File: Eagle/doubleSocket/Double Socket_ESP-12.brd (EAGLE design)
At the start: 160 x 100 mm, 29 parts, among them IC1 LM1117IMPX-3.3, K1 G5L, K2 G5L, T1 2N3904, T2 2N3904

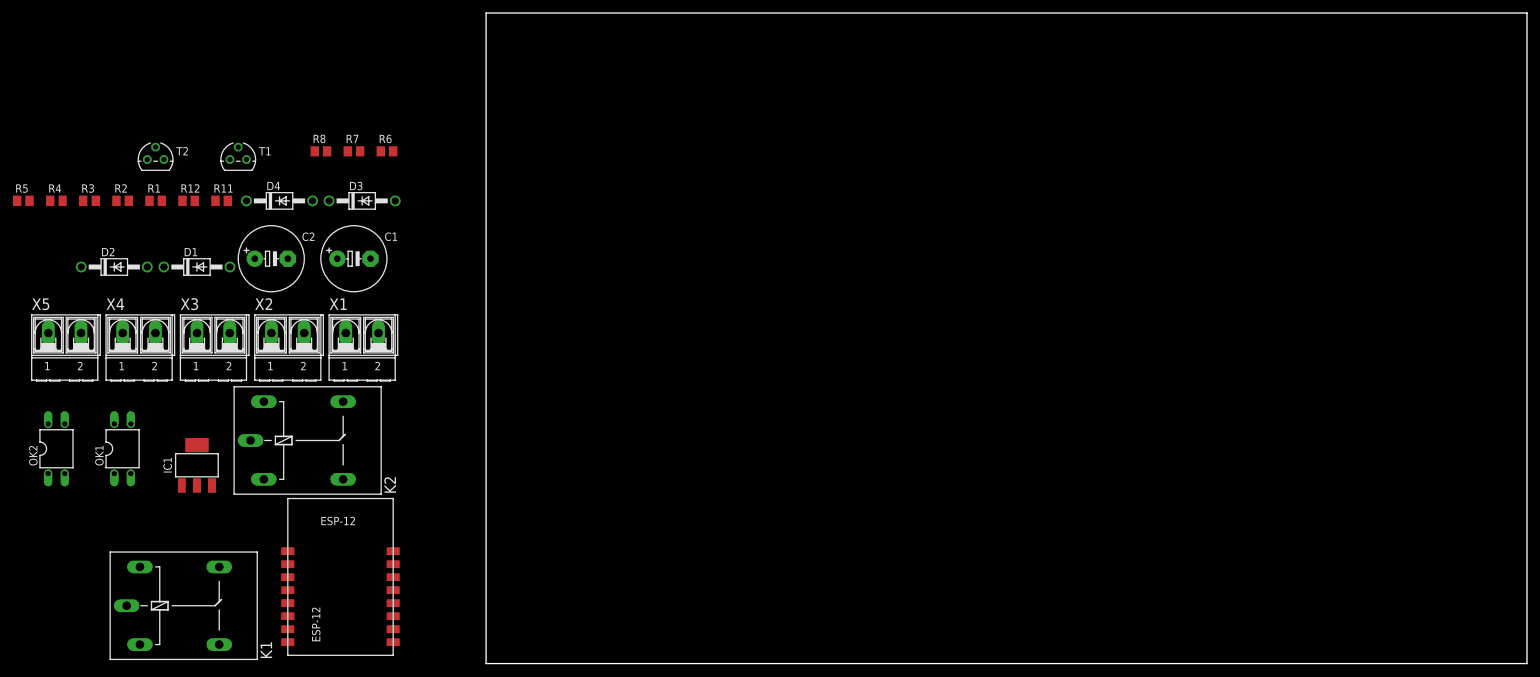
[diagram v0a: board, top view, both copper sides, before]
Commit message: Updated gitignore
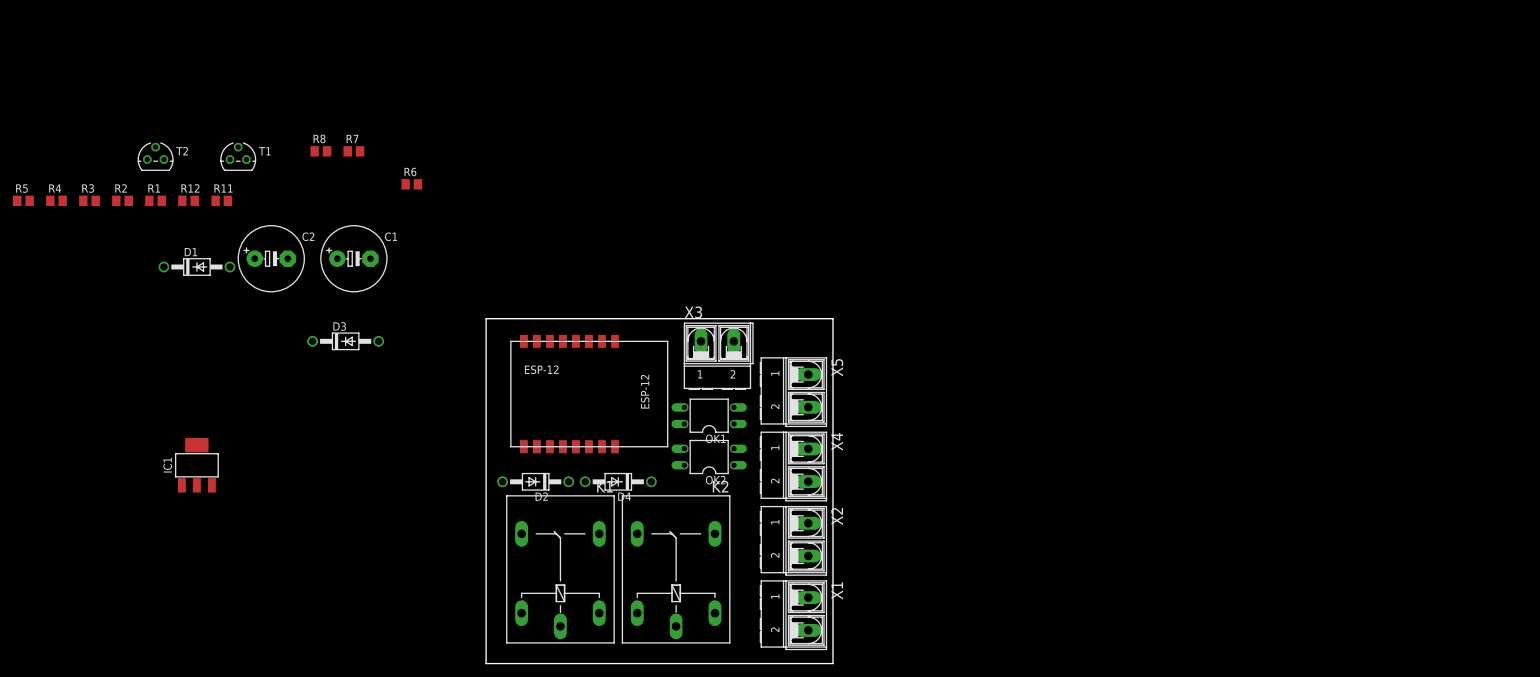
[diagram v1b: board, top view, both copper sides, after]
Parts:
- moved X5 114.6 mm to (49.5, 41.9), turned to 270 degrees
- moved X4 104.9 mm to (49.5, 30.5), turned to 270 degrees
- moved OK2 100.3 mm to (34.3, 31.8), turned to 90 degrees
- moved OK1 90.3 mm to (34.3, 38.1), turned to 90 degrees
- moved X2 86.1 mm to (49.5, 19.1), turned to 270 degrees
- moved X1 81.0 mm to (49.5, 7.62), turned to 270 degrees
- moved X3 77.5 mm to (35.6, 49.5)
- moved D2 72.7 mm to (7.62, 27.9), turned to 180 degrees
- moved D4 67.6 mm to (20.3, 27.9), turned to 180 degrees
- moved K2 59.0 mm to (29.2, 15.2), turned to 90 degrees
- moved K1 57.5 mm to (11.4, 15.2), turned to 90 degrees
- moved ESP-12 48.0 mm to (15.2, 41.9), turned to 270 degrees
- moved D3 21.7 mm to (-21.6, 49.5)
- moved R6 6.35 mm to (-11.4, 73.7)
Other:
- board size 160 x 100 mm -> 53.3 x 53 mm

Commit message: temp version
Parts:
- removed C1: 100, rcl:E5-10,5
- removed C2: 1000, rcl:E5-10,5
- added C3: 100uF, rcl:C0805
- added C4: 1000uF, rcl:C0805
- added U$1: HLK-PM01, aobotelhoLibrary:HLK-PM01
- moved T2 123.7 mm to (49.5, 5.08), turned to 90 degrees
- moved R5 115.3 mm to (33.0, 21.6), turned to 180 degrees
- moved T1 108.2 mm to (49.5, 14.0), turned to 90 degrees
- moved R2 106.7 mm to (31.8, 10.2)
- moved R8 100.6 mm to (43.2, 5.08)
- moved R1 95.5 mm to (26.7, 15.2), turned to 270 degrees
- moved D1 92.4 mm to (34.3, 12.7)
- moved IC1 91.8 mm to (44.5, 53.3), turned to 270 degrees
- moved R7 89.3 mm to (36.8, 10.2), turned to 180 degrees
- moved R4 88.9 mm to (10.2, 25.4)
- moved R6 80.9 mm to (43.2, 14.0)
- moved R3 79.0 mm to (10.2, 36.8), turned to 180 degrees
- moved R12 76.8 mm to (14.0, 22.9), turned to 180 degrees
- moved R11 74.6 mm to (14.0, 20.3), turned to 180 degrees
- moved D3 73.8 mm to (34.3, 1.27)
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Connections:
- net N$10 renamed OPTO_LED-1
- net N$3 renamed OPTO_LED+2
- net N$4 renamed OPT_EMITTER2
- net N$5 renamed OPT_LED-2
- net N$6 renamed OPTO_LED+1
- net N$9 renamed OPTO_EMITTER1
- removed net N$1: K1.P, X1.2
- removed net N$15: K2.P, X2.2
- new net AC1: K1.P, K2.P, U$1.AC1, X3.2
- new net AC2: U$1.AC2, X1.2, X2.2, X3.1
- net 5V: now also C3.1, U$1.VO+; no longer C1.+, X3.2
- net GND: now also C3.2, C4.2, U$1.VO-; no longer C1.-, C2.-, X3.1
- net VCC: now also C4.1; no longer C2.+
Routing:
- net AC1: track 0.00 -> 67.5 mm
- net N$14: track 0.00 -> 54.3 mm, vias 0 -> 5
- net AC2: track 0.00 -> 46.6 mm
- net OUTPUT1: track 0.00 -> 28.0 mm
- net N$2: track 0.00 -> 28.0 mm
- net VCC: track 0.00 -> 13.2 mm
- net 5V: track 0.00 -> 9.94 mm
- added copper zone on layer 1, net GND
- added copper zone on layer 16, net GND
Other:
- board size 53.3 x 53 mm -> 53.3 x 80 mm
